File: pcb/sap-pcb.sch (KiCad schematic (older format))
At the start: 17 parts, among them U1 Arduino_Nano

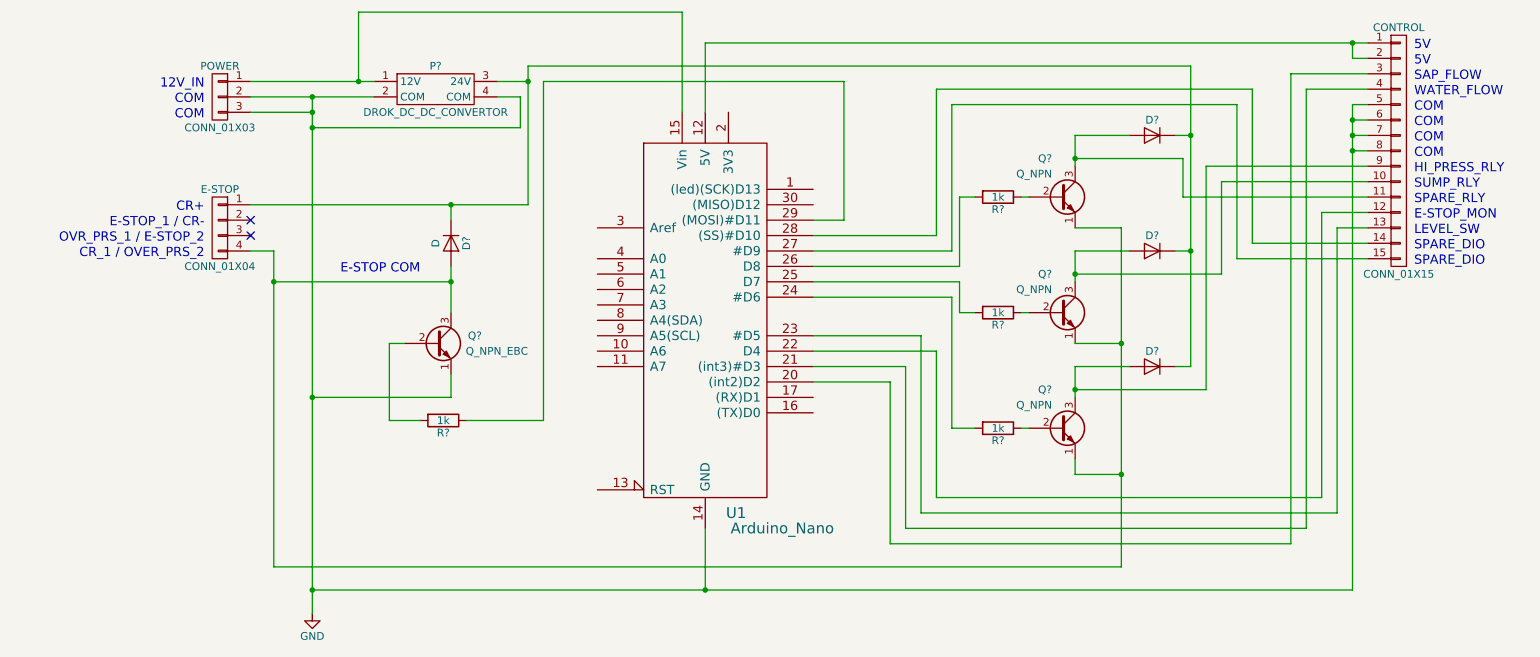
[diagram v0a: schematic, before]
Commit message: finished kicad components.
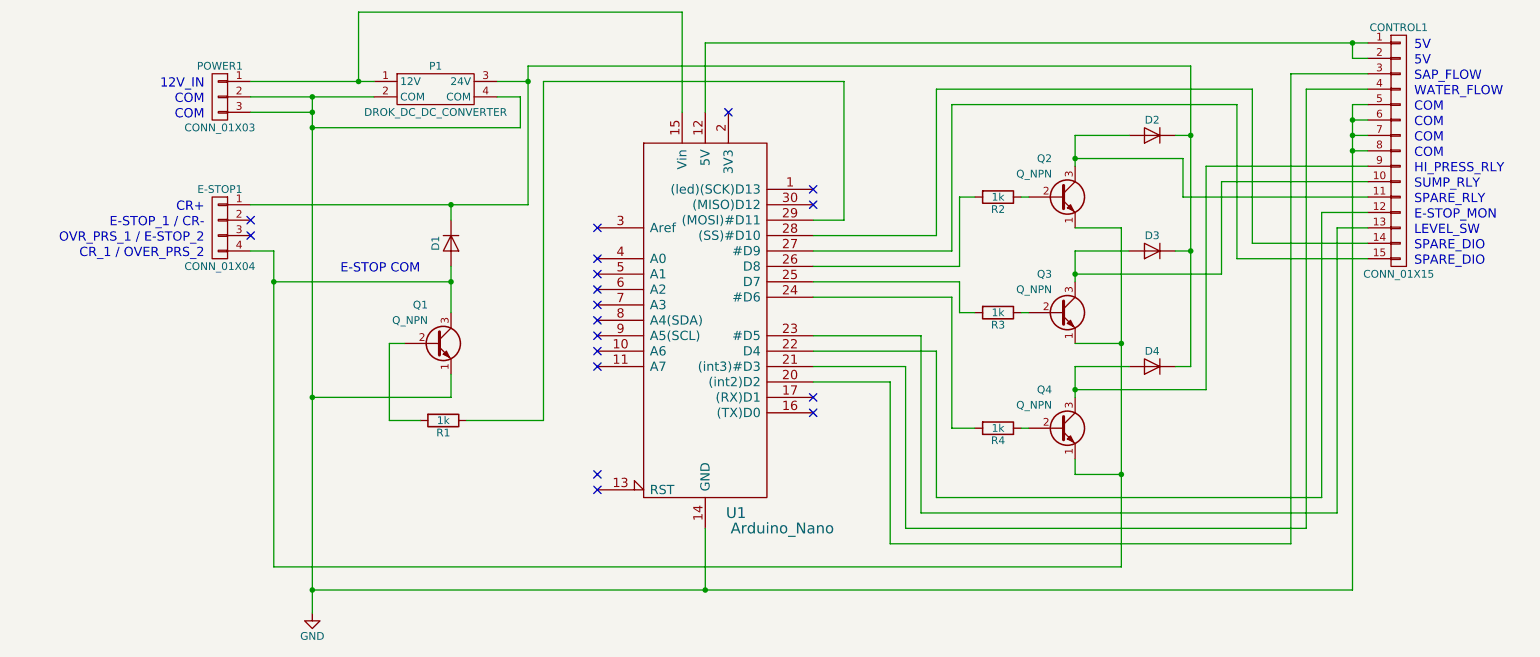
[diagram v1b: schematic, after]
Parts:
- removed D?: D, symbol D
- removed Q?: Q_NPN_EBC, TO_SOT_Packages_THT:TO-92_Molded_Narrow, symbol Q_NPN_EBC
- removed Q? (x3): Q_NPN, TO_SOT_Packages_THT:TO-92_Molded_Narrow, symbol Q_NPN_EBC
- removed R? (x3): 1k, Resistors_ThroughHole:Resistor_Horizontal_RM10mm, symbol R
- added D1: D, Diodes_ThroughHole:D_A-405_P10.16mm_Horizontal, symbol D
- added Q1, Q2, Q3, Q4: Q_NPN, sap-pcb:TRANSISTOR, symbol Q_NPN_EBC
- added R2, R3, R4: 1k, Resistors_ThroughHole:R_Axial_DIN0207_L6.3mm_D2.5mm_P10.16mm_Horizontal, symbol R
- CONTROL1: renamed from CONTROL; footprint (none) -> sap-pcb:15-PIN_CONN
- D2, D3, D4: renamed from D?; footprint Diodes_ThroughHole:Diode_DO-41_SOD81_Horizontal_RM10 -> Diodes_ThroughHole:D_A-405_P10.16mm_Horizontal
- E-STOP1: renamed from E-STOP; footprint USBdio-PCB:PHX_HDR_4_POS_(1933202) -> sap-pcb:4-PIN_CONN
- P1: renamed from P?; value DROK_DC_DC_CONVERTOR -> DROK_DC_DC_CONVERTER; footprint (none) -> sap-pcb:DROK_DC_DC_CONVERTER
- POWER1: renamed from POWER; footprint (none) -> sap-pcb:3-PIN_CONN
- R1: renamed from R?; footprint (none) -> Resistors_ThroughHole:R_Axial_DIN0207_L6.3mm_D2.5mm_P10.16mm_Horizontal
- U1: footprint USBdio-PCB:ARDUINO_NANO -> sap-pcb:ARDUINO_NANO
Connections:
- net GND: now also Q1.1 (E)
- net at U1.24 (#D6): now also R4.2
- net at U1.25 (D7): now also R3.2
- net at U1.26 (D8): now also R2.2
- net at D2.1 (K), D3.1 (K), D4.1 (K)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: now also D1.1 (K)
- net at E-STOP1.4 (P4): now also D1.2 (A), Q1.3 (C), Q2.1 (E), Q3.1 (E), Q4.1 (E)
- net at CONTROL1.10 (P10), D3.2 (A): now also Q3.3 (C)
- net at CONTROL1.11 (P11), D2.2 (A): now also Q2.3 (C)
- net at CONTROL1.9 (P9), D4.2 (A): now also Q4.3 (C)
- net at R1.2: now also Q1.2 (B)
- new net: Q2.2 (B), R2.1
- new net: Q3.2 (B), R3.1
- new net: Q4.2 (B), R4.1
- no-connect marks 2 -> 18
